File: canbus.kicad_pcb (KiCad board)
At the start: 2 copper layers, 34.5 x 37.6 mm, 15 parts, among them J1 Conn_01x08, J2 RJ45, J3 RJ45, U1 MCP2515-E/SO, U2 MCP2562-H/SN, Y1 Crystal_GND24

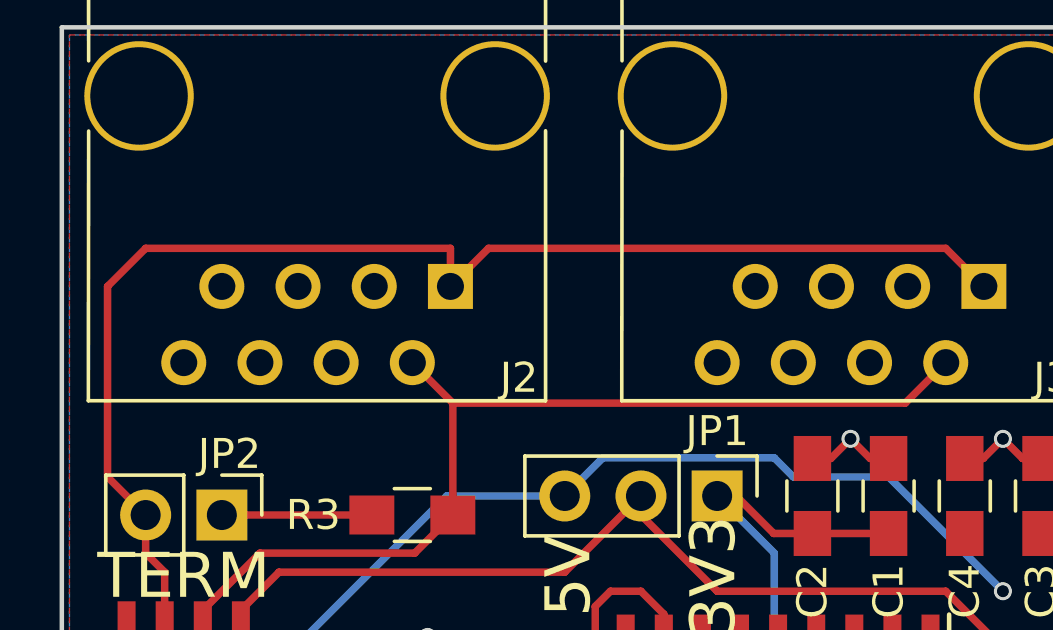
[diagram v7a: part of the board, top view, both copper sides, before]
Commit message: Added gnd to RJ45 and connected all pins for passthrough
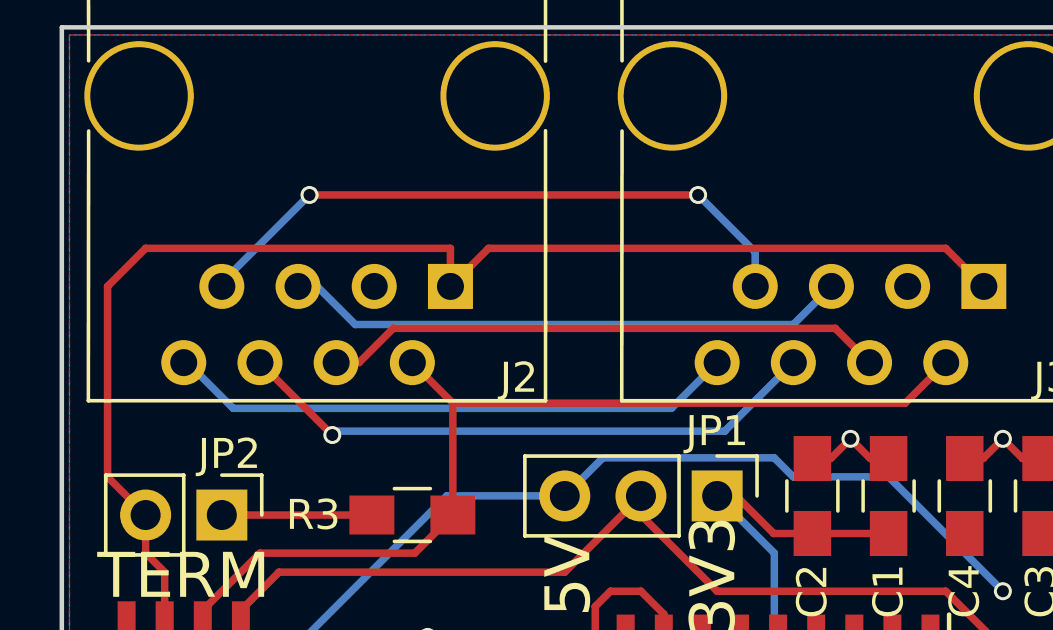
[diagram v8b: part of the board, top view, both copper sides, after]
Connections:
- J2 pad 3: Net-(J2-Pad3) -> GND
- J3 pad 3: Net-(J3-Pad3) -> GND
- J3 pad 4: Net-(J3-Pad4) -> Net-(J2-Pad4)
- J3 pad 5: Net-(J3-Pad5) -> Net-(J2-Pad5)
- J3 pad 6: Net-(J3-Pad6) -> Net-(J2-Pad6)
- J3 pad 7: Net-(J3-Pad7) -> Net-(J2-Pad7)
- J3 pad 8: Net-(J3-Pad8) -> Net-(J2-Pad8)
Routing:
- net Net-(J2-Pad7): track 0.00 -> 21.0 mm, vias 0 -> 2
- net Net-(J2-Pad6): track 0.00 -> 19.8 mm, vias 0 -> 1
- net Net-(J2-Pad5): track 0.00 -> 19.2 mm
- net Net-(J2-Pad8): track 0.00 -> 19.0 mm
- net Net-(J2-Pad4): track 0.00 -> 18.7 mm
